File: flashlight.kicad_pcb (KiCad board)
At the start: 2 copper layers, 46 x 122 mm, 63 parts, among them J11 USB_C_Receptacle_USB2.0_16P, Q2 HSS2333, U1 XB4908A, U2 MT3608, U3 TP5000, U4 R6BHC-A05_LED-19-223, U5 SS12J01_071

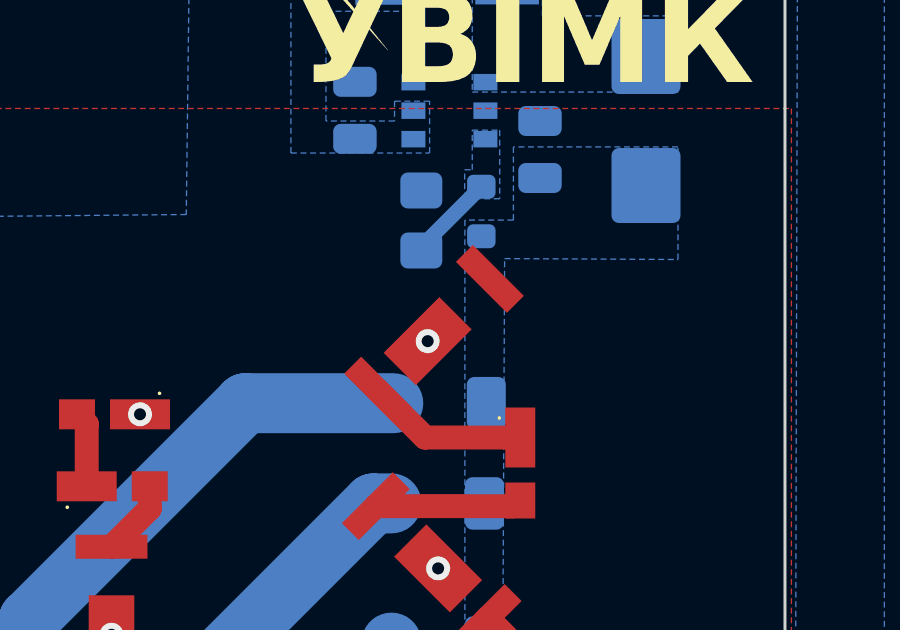
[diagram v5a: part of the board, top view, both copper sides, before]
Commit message: Added an extra out capacitor
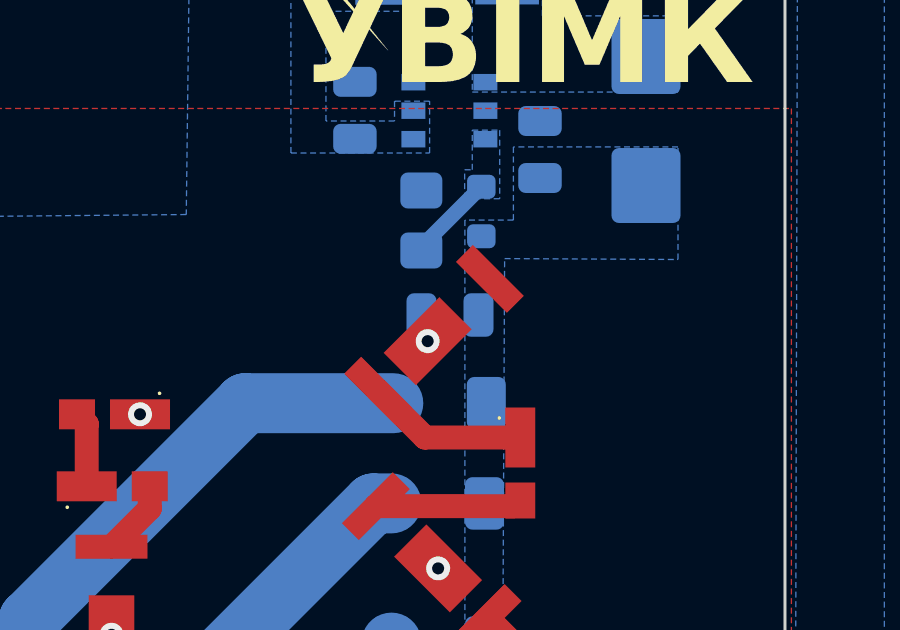
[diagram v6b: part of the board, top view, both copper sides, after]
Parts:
- added C7: 22uF/35V, Capacitor_SMD:C_0805_2012Metric, B.Cu at (106.9, 94.1)
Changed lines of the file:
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@@
+		)
+	)
+	(footprint "Capacitor_SMD:C_0805_2012Metric"
+		(layer "B.Cu")
+		(at 106.934 94.064 180)
+		(descr "Capacitor SMD 0805 (2012 Metric), square (rectangular) end terminal, IPC-7351 nominal, (Body size source: IPC-SM-782 page 76, https://www.pcb-3d.com/wordpress/wp-content/uploads/ipc-sm-782a_amendment_1_and_2.pdf, https://docs.google.com/spreadsheets/d/1BsfQQcO9C6DZCsRaXUlFlo91Tg2WpOkGARC1WS5S8t0/edit?usp=sharing), generated with kicad-footprint-generator")
+		(tags "capacitor")
+		(property "Reference" "C7"
+			(at 0 1.68 0)
+			(layer "B.Fab")
+			(effects
+				(font
+					(size 1 1)
+					(thickness 0.15)
+				)
+				(justify mirror)
+			)
+		)
+		(property "Value" "22uF/35V"
+			(at 0 -1.68 0)
+			(layer "B.Fab")
+			(effects
+				(font
+					(size 1 1)
+					(thickness 0.15)
+				)
+				(justify mirror)
+			)
+		)
+		(property "Datasheet" "~"
+			(at 0 0 0)
+			(layer "B.Fab")
+			(hide yes)
+			(effects
+				(font
+					(size 1.27 1.27)
+					(thickness 0.15)
+				)
+				(justify mirror)
+			)
+		)
+		(property "Description" "Unpolarized capacitor"
+			(at 0 0 0)
+			(layer "B.Fab")
+			(hide yes)
+			(effects
+				(font
+					(size 1.27 1.27)
+					(thickness 0.15)
+				)
+				(justify mirror)
+			)
+		)
+		(property "LCSC" "C6119901"
+			(at 0 0 0)
+			(unlocked yes)
+			(layer "B.Fab")
+			(hide yes)
+			(effects
+				(font
+					(size 1 1)
+					(thickness 0.15)
+				)
+				(justify mirror)
+			)
+		)
+		(property ki_fp_filters "C_*")
+		(sheetname "/")
+		(sheetfile "flashlight.kicad_sch")
+		(attr smd)
+		(fp_line
+			(start -0.261252 0.735)
+			(end 0.261252 0.735)
+			(stroke
+				(width 0.12)
+				(type solid)
+			)
+			(layer "B.SilkS")
+		)
+		(fp_line
+			(start -0.261252 -0.735)
+			(end 0.261252 -0.735)
+			(stroke
+				(width 0.12)
+				(type solid)
+			)
+			(layer "B.SilkS")
+		)
+		(fp_line
+			(start 1.7 0.98)
+			(end 1.7 -0.98)
+			(stroke
+				(width 0.05)
+				(type solid)
+			)
+			(layer "B.CrtYd")
+		)
+		(fp_line
+			(start 1.7 -0.98)
+			(end -1.7 -0.98)
+			(stroke
+				(width 0.05)
+				(type solid)
+			)
+			(layer "B.CrtYd")
+		)
+		(fp_line
+			(start -1.7 0.98)
+			(end 1.7 0.98)
+			(stroke
+				(width 0.05)
+				(type solid)
+			)
+			(layer "B.CrtYd")
+		)
+		(fp_line
+			(start -1.7 -0.98)
+			(end -1.7 0.98)
+			(stroke
+				(width 0.05)
+				(type solid)
+			)
+			(layer "B.CrtYd")
+		)
+		(fp_line
+			(start 1 0.625)
+			(end 1 -0.625)
+			(stroke
+				(width 0.1)
+				(type solid)
+			)
+			(layer "B.Fab")
+		)
+		(fp_line
+			(start 1 -0.625)
+			(end -1 -0.625)
+			(stroke
+				(width 0.1)
+				(type solid)
+			)
+			(layer "B.Fab")
+		)
+		(fp_line
+			(start -1 0.625)
+			(end 1 0.625)
+			(stroke
+				(width 0.1)
+				(type solid)
+			)
+			(layer "B.Fab")
+		)
+		(fp_line
+			(start -1 -0.625)
+			(end -1 0.625)
+			(stroke
+				(width 0.1)
+				(type solid)
+			)
+			(layer "B.Fab")
+		)
+		(fp_text user "${REFERENCE}"
+			(at 0 0 0)
+			(layer "B.Fab")
+			(effects
+				(font
+					(size 0.5 0.5)
+					(thickness 0.08)
+				)
+				(justify mirror)
+			)
+		)
+		(pad "1" smd roundrect
+			(at -0.95 0 180)
+			(size 1 1.45)
+			(layers "B.Cu" "B.Mask" "B.Paste")
+			(roundrect_rratio 0.25)
+			(net 4 "VOUT")
+			(pintype "passive")
+		)
+		(pad "2" smd roundrect
+			(at 0.95 0 180)
+			(size 1 1.45)
+			(layers "B.Cu" "B.Mask" "B.Paste")
+			(roundrect_rratio 0.25)
+			(net 11 "Earth_Protective")
+			(pintype "passive")
+		)
+		(embedded_fonts no)
+		(model "${KICAD9_3DMODEL_DIR}/Capacitor_SMD.3dshapes/C_0805_2012Metric.step"
+			(offset
+				(xyz 0 0 0)
+			)
+			(scale
+				(xyz 1 1 1)
+			)
+			(rotate
+				(xyz 0 0 0)
+			)
 		)
 	)
